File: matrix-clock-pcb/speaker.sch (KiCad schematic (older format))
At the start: 10 parts

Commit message: pcb: update pcb files
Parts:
- gave numbers to parts that had none: 10
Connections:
- net +3V3 renamed +5V
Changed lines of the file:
@@
 $EndDescr
 $Comp
-L Device:C C?
+L Device:C C14
 U 1 1 5F381B14
 P 5100 3900
-F 0 "C?" V 5050 3800 50  0000 C CNN
+F 0 "C14" V 5050 3800 50  0000 C CNN
 F 1 "1uf" V 4939 3900 50  0000 C CNN
 F 2 "Capacitor_SMD:C_0402_1005Metric" H 5138 3750 50  0001 C CNN
@@
 $EndComp
 $Comp
-L Device:R R?
+L Device:R R13
 U 1 1 5F3825B3
 P 5800 4250
-F 0 "R?" V 5700 4250 50  0000 C CNN
+F 0 "R13" V 5700 4250 50  0000 C CNN
 F 1 "20k" V 5900 4250 50  0000 C CNN
 F 2 "Resistor_SMD:R_0402_1005Metric" V 5730 4250 50  0001 C CNN
@@
 	5400 4000 5400 4250
 $Comp
-L Connector_Generic:Conn_01x02 J?
+L Connector_Generic:Conn_01x02 J5
 U 1 1 5F38725C
 P 6900 3900
-F 0 "J?" H 6980 3892 50  0000 L CNN
+F 0 "J5" H 6980 3892 50  0000 L CNN
 F 1 "Speaker" H 6980 3801 50  0000 L CNN
 F 2 "Connector_PinHeader_2.54mm:PinHeader_1x02_P2.54mm_Vertical" H 6900 3900 50  0001 C CNN
@@
 	5650 4250 5400 4250
 $Comp
-L Device:R R?
+L Device:R R12
 U 1 1 5F388BFA
 P 5250 4250
-F 0 "R?" V 5150 4250 50  0000 C CNN
+F 0 "R12" V 5150 4250 50  0000 C CNN
 F 1 "20k" V 5350 4250 50  0000 C CNN
 F 2 "Resistor_SMD:R_0402_1005Metric" V 5180 4250 50  0001 C CNN
@@
 Connection ~ 5400 4250
 $Comp
-L Device:C C?
+L Device:C C13
 U 1 1 5F389470
 P 4950 4250
-F 0 "C?" V 4900 4350 50  0000 C CNN
+F 0 "C13" V 4900 4350 50  0000 C CNN
 F 1 "0.39uf" V 4789 4250 50  0000 C CNN
 F 2 "Capacitor_SMD:C_0402_1005Metric" H 4988 4100 50  0001 C CNN
@@
 INPUT
 $Comp
-L power:GND #PWR?
+L power:GND #PWR0136
 U 1 1 5F38A0EB
 P 6100 3800
-F 0 "#PWR?" H 6100 3550 50  0001 C CNN
+F 0 "#PWR0136" H 6100 3550 50  0001 C CNN
 F 1 "GND" V 6105 3672 50  0000 R CNN
 F 2 "" H 6100 3800 50  0001 C CNN
@@
 $EndComp
 $Comp
-L power:GND #PWR?
+L power:GND #PWR0137
 U 1 1 5F38A766
 P 4950 3900
-F 0 "#PWR?" H 4950 3650 50  0001 C CNN
+F 0 "#PWR0137" H 4950 3650 50  0001 C CNN
 F 1 "GND" V 4955 3772 50  0000 R CNN
 F 2 "" H 4950 3900 50  0001 C CNN
@@
 $EndBitmap
 $Comp
-L mylib:TC8002D U?
+L mylib:TC8002D U7
 U 1 1 5F5572A6
 P 5750 3850
-F 0 "U?" H 5800 4225 50  0000 C CNN
+F 0 "U7" H 5800 4225 50  0000 C CNN
 F 1 "TC8002D" H 5800 4134 50  0000 C CNN
 F 2 "Package_SO:SOIC-8_3.9x4.9mm_P1.27mm" H 5850 3850 50  0001 C CNN
@@
 $EndComp
 $Comp
-L power:+3.3V #PWR?
-U 1 1 5F558480
-P 6100 3900
-F 0 "#PWR?" H 6100 3750 50  0001 C CNN
-F 1 "+3.3V" V 6115 4028 50  0000 L CNN
-F 2 "" H 6100 3900 50  0001 C CNN
-F 3 "" H 6100 3900 50  0001 C CNN
-	1    6100 3900
-	0    1    1    0
-$EndComp
-$Comp
-L Device:C C?
+L Device:C C11
 U 1 1 5F55C734
 P 4200 4550
-F 0 "C?" H 4250 4450 50  0000 C CNN
+F 0 "C11" H 4250 4450 50  0000 C CNN
 F 1 "0.39uf" H 4050 4650 50  0000 C CNN
 F 2 "Capacitor_SMD:C_0402_1005Metric" H 4238 4400 50  0001 C CNN
@@
 $EndComp
 $Comp
-L Device:R R?
+L Device:R R10
 U 1 1 5F55CDA5
 P 4050 4250
-F 0 "R?" V 3950 4250 50  0000 C CNN
+F 0 "R10" V 3950 4250 50  0000 C CNN
 F 1 "20k" V 4150 4250 50  0000 C CNN
 F 2 "Resistor_SMD:R_0402_1005Metric" V 3980 4250 50  0001 C CNN
@@
 $EndComp
 $Comp
-L Device:R R?
+L Device:R R11
 U 1 1 5F55D483
 P 4450 4250
-F 0 "R?" V 4350 4250 50  0000 C CNN
+F 0 "R11" V 4350 4250 50  0000 C CNN
 F 1 "20k" V 4550 4250 50  0000 C CNN
 F 2 "Resistor_SMD:R_0402_1005Metric" V 4380 4250 50  0001 C CNN
@@
 $EndComp
 $Comp
-L Device:C C?
+L Device:C C12
 U 1 1 5F55D853
 P 4600 4550
-F 0 "C?" H 4650 4450 50  0000 C CNN
+F 0 "C12" H 4650 4450 50  0000 C CNN
 F 1 "0.39uf" H 4450 4650 50  0000 C CNN
 F 2 "Capacitor_SMD:C_0402_1005Metric" H 4638 4400 50  0001 C CNN
@@
 	4600 4800 4600 4700
 $Comp
-L power:GND #PWR?
+L power:GND #PWR0139
 U 1 1 5F55FC0C
 P 4400 4800
-F 0 "#PWR?" H 4400 4550 50  0001 C CNN
+F 0 "#PWR0139" H 4400 4550 50  0001 C CNN
 F 1 "GND" V 4405 4672 50  0000 R CNN
 F 2 "" H 4400 4800 50  0001 C CNN
@@
 Wire Wire Line
 	4400 4800 4600 4800
+$Comp
+L power:+5V #PWR0138
+U 1 1 5FACCCCA
+P 6100 3900
+F 0 "#PWR0138" H 6100 3750 50  0001 C CNN
+F 1 "+5V" V 6115 4028 50  0000 L CNN
+F 2 "" H 6100 3900 50  0001 C CNN
+F 3 "" H 6100 3900 50  0001 C CNN
+	1    6100 3900
+	0    1    1    0
+$EndComp
 $EndSCHEMATC

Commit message: pcb: update pcb to v1.1
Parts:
- R12: value 20k -> 10k
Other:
- moved on the sheet: C11, C12, C13, C14, J5, R10, R11, R12, R13, U7
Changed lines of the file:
@@
 L Device:C C14
 U 1 1 5F381B14
-P 5100 3900
-F 0 "C14" V 5050 3800 50  0000 C CNN
-F 1 "1uf" V 4939 3900 50  0000 C CNN
-F 2 "Capacitor_SMD:C_0402_1005Metric" H 5138 3750 50  0001 C CNN
-F 3 "~" H 5100 3900 50  0001 C CNN
-	1    5100 3900
+P 6300 3800
+F 0 "C14" V 6250 3700 50  0000 C CNN
+F 1 "1uf" V 6139 3800 50  0000 C CNN
+F 2 "Capacitor_SMD:C_0402_1005Metric" H 6338 3650 50  0001 C CNN
+F 3 "~" H 6300 3800 50  0001 C CNN
+	1    6300 3800
 	0    1    1    0
 $EndComp
@@
 L Device:R R13
 U 1 1 5F3825B3
-P 5800 4250
-F 0 "R13" V 5700 4250 50  0000 C CNN
-F 1 "20k" V 5900 4250 50  0000 C CNN
-F 2 "Resistor_SMD:R_0402_1005Metric" V 5730 4250 50  0001 C CNN
-F 3 "~" H 5800 4250 50  0001 C CNN
-	1    5800 4250
+P 7000 4150
+F 0 "R13" V 6900 4150 50  0000 C CNN
+F 1 "20k" V 7100 4150 50  0000 C CNN
+F 2 "Resistor_SMD:R_0402_1005Metric" V 6930 4150 50  0001 C CNN
+F 3 "~" H 7000 4150 50  0001 C CNN
+	1    7000 4150
 	0    1    1    0
 $EndComp
 Wire Wire Line
-	5500 3800 5250 3800
-Wire Wire Line
-	5250 3800 5250 3900
-Wire Wire Line
-	5250 3900 5500 3900
-Connection ~ 5250 3900
-Text HLabel 4800 3700 0    50   Input ~ 0
+	6700 3700 6450 3700
+Wire Wire Line
+	6450 3700 6450 3800
+Wire Wire Line
+	6450 3800 6700 3800
+Connection ~ 6450 3800
+Text HLabel 6000 3600 0    50   Input ~ 0
 SHUTDOWN
 Wire Wire Line
-	5500 4000 5400 4000
-Wire Wire Line
-	5400 4000 5400 4250
+	6700 3900 6600 3900
+Wire Wire Line
+	6600 3900 6600 4150
 $Comp
 L Connector_Generic:Conn_01x02 J5
 U 1 1 5F38725C
-P 6900 3900
-F 0 "J5" H 6980 3892 50  0000 L CNN
-F 1 "Speaker" H 6980 3801 50  0000 L CNN
-F 2 "Connector_PinHeader_2.54mm:PinHeader_1x02_P2.54mm_Vertical" H 6900 3900 50  0001 C CNN
-F 3 "~" H 6900 3900 50  0001 C CNN
-	1    6900 3900
+P 8100 3800
+F 0 "J5" H 8180 3792 50  0000 L CNN
+F 1 "Speaker" H 8180 3701 50  0000 L CNN
+F 2 "Connector_PinHeader_2.54mm:PinHeader_1x02_P2.54mm_Vertical" H 8100 3800 50  0001 C CNN
+F 3 "~" H 8100 3800 50  0001 C CNN
+	1    8100 3800
 	1    0    0    -1
 $EndComp
 Wire Wire Line
-	6700 4000 6250 4000
-Wire Wire Line
-	6100 3700 6600 3700
-Wire Wire Line
-	6600 3700 6600 3900
-Wire Wire Line
-	6600 3900 6700 3900
-Wire Wire Line
-	5950 4250 6250 4250
-Wire Wire Line
-	6250 4250 6250 4000
-Connection ~ 6250 4000
-Wire Wire Line
-	6250 4000 6100 4000
-Wire Wire Line
-	5650 4250 5400 4250
+	7900 3900 7450 3900
+Wire Wire Line
+	7300 3600 7800 3600
+Wire Wire Line
+	7800 3600 7800 3800
+Wire Wire Line
+	7800 3800 7900 3800
+Wire Wire Line
+	7150 4150 7450 4150
+Wire Wire Line
+	7450 4150 7450 3900
+Connection ~ 7450 3900
+Wire Wire Line
+	7450 3900 7300 3900
+Wire Wire Line
+	6850 4150 6600 4150
 $Comp
 L Device:R R12
 U 1 1 5F388BFA
-P 5250 4250
-F 0 "R12" V 5150 4250 50  0000 C CNN
-F 1 "20k" V 5350 4250 50  0000 C CNN
-F 2 "Resistor_SMD:R_0402_1005Metric" V 5180 4250 50  0001 C CNN
-F 3 "~" H 5250 4250 50  0001 C CNN
-	1    5250 4250
+P 6450 4150
+F 0 "R12" V 6350 4150 50  0000 C CNN
+F 1 "10k" V 6550 4150 50  0000 C CNN
+F 2 "Resistor_SMD:R_0402_1005Metric" V 6380 4150 50  0001 C CNN
+F 3 "~" H 6450 4150 50  0001 C CNN
+	1    6450 4150
 	0    1    1    0
 $EndComp
-Connection ~ 5400 4250
+Connection ~ 6600 4150
 $Comp
 L Device:C C13
 U 1 1 5F389470
-P 4950 4250
-F 0 "C13" V 4900 4350 50  0000 C CNN
-F 1 "0.39uf" V 4789 4250 50  0000 C CNN
-F 2 "Capacitor_SMD:C_0402_1005Metric" H 4988 4100 50  0001 C CNN
-F 3 "~" H 4950 4250 50  0001 C CNN
-	1    4950 4250
+P 6150 4150
+F 0 "C13" V 6100 4250 50  0000 C CNN
+F 1 "0.39uf" V 5989 4150 50  0000 C CNN
+F 2 "Capacitor_SMD:C_0402_1005Metric" H 6188 4000 50  0001 C CNN
+F 3 "~" H 6150 4150 50  0001 C CNN
+	1    6150 4150
 	0    1    1    0
 $EndComp
-Text HLabel 3900 4250 0    50   Input ~ 0
+Text HLabel 5100 4150 0    50   Input ~ 0
 INPUT
 $Comp
 L power:GND #PWR0136
 U 1 1 5F38A0EB
-P 6100 3800
-F 0 "#PWR0136" H 6100 3550 50  0001 C CNN
-F 1 "GND" V 6105 3672 50  0000 R CNN
-F 2 "" H 6100 3800 50  0001 C CNN
-F 3 "" H 6100 3800 50  0001 C CNN
-	1    6100 3800
+P 7300 3700
+F 0 "#PWR0136" H 7300 3450 50  0001 C CNN
+F 1 "GND" V 7305 3572 50  0000 R CNN
+F 2 "" H 7300 3700 50  0001 C CNN
+F 3 "" H 7300 3700 50  0001 C CNN
+	1    7300 3700
 	0    -1   -1   0
 $EndComp
@@
 L power:GND #PWR0137
 U 1 1 5F38A766
-P 4950 3900
-F 0 "#PWR0137" H 4950 3650 50  0001 C CNN
-F 1 "GND" V 4955 3772 50  0000 R CNN
-F 2 "" H 4950 3900 50  0001 C CNN
-F 3 "" H 4950 3900 50  0001 C CNN
-	1    4950 3900
+P 6150 3800
+F 0 "#PWR0137" H 6150 3550 50  0001 C CNN
+F 1 "GND" V 6155 3672 50  0000 R CNN
+F 2 "" H 6150 3800 50  0001 C CNN
+F 3 "" H 6150 3800 50  0001 C CNN
+	1    6150 3800
 	0    1    1    0
 $EndComp
 Wire Wire Line
-	4800 3700 5500 3700
+	6000 3600 6700 3600
 $Bitmap
-Pos 1900 4000
+Pos 3100 3900
 Scale 1.500000
 Data
@@
 L mylib:TC8002D U7
 U 1 1 5F5572A6
-P 5750 3850
-F 0 "U7" H 5800 4225 50  0000 C CNN
-F 1 "TC8002D" H 5800 4134 50  0000 C CNN
-F 2 "Package_SO:SOIC-8_3.9x4.9mm_P1.27mm" H 5850 3850 50  0001 C CNN
-F 3 "" H 5750 3850 50  0001 C CNN
-	1    5750 3850
+P 6950 3750
+F 0 "U7" H 7000 4125 50  0000 C CNN
+F 1 "TC8002D" H 7000 4034 50  0000 C CNN
+F 2 "Package_SO:SOIC-8_3.9x4.9mm_P1.27mm" H 7050 3750 50  0001 C CNN
+F 3 "" H 6950 3750 50  0001 C CNN
+	1    6950 3750
 	1    0    0    -1
 $EndComp
@@
 L Device:C C11
 U 1 1 5F55C734
-P 4200 4550
-F 0 "C11" H 4250 4450 50  0000 C CNN
-F 1 "0.39uf" H 4050 4650 50  0000 C CNN
-F 2 "Capacitor_SMD:C_0402_1005Metric" H 4238 4400 50  0001 C CNN
-F 3 "~" H 4200 4550 50  0001 C CNN
-	1    4200 4550
+P 5400 4450
+F 0 "C11" H 5450 4350 50  0000 C CNN
+F 1 "0.39uf" H 5250 4550 50  0000 C CNN
+F 2 "Capacitor_SMD:C_0402_1005Metric" H 5438 4300 50  0001 C CNN
+F 3 "~" H 5400 4450 50  0001 C CNN
+	1    5400 4450
 	-1   0    0    1
 $EndComp
@@
 L Device:R R10
 U 1 1 5F55CDA5
-P 4050 4250
-F 0 "R10" V 3950 4250 50  0000 C CNN
-F 1 "20k" V 4150 4250 50  0000 C CNN
-F 2 "Resistor_SMD:R_0402_1005Metric" V 3980 4250 50  0001 C CNN
-F 3 "~" H 4050 4250 50  0001 C CNN
-	1    4050 4250
-	0    1    1    0
-$EndComp
-$Comp
-L Device:R R11
-U 1 1 5F55D483
-P 4450 4250
-F 0 "R11" V 4350 4250 50  0000 C CNN
-F 1 "20k" V 4550 4250 50  0000 C CNN
-F 2 "Resistor_SMD:R_0402_1005Metric" V 4380 4250 50  0001 C CNN
-F 3 "~" H 4450 4250 50  0001 C CNN
-	1    4450 4250
+P 5250 4150
+F 0 "R10" V 5150 4150 50  0000 C CNN
+F 1 "20k" V 5350 4150 50  0000 C CNN
+F 2 "Resistor_SMD:R_0402_1005Metric" V 5180 4150 50  0001 C CNN
+F 3 "~" H 5250 4150 50  0001 C CNN
+	1    5250 4150
 	0    1    1    0
 $EndComp
@@
 L Device:C C12
 U 1 1 5F55D853
-P 4600 4550
-F 0 "C12" H 4650 4450 50  0000 C CNN
-F 1 "0.39uf" H 4450 4650 50  0000 C CNN
-F 2 "Capacitor_SMD:C_0402_1005Metric" H 4638 4400 50  0001 C CNN
-F 3 "~" H 4600 4550 50  0001 C CNN
-	1    4600 4550
+P 5800 4450
+F 0 "C12" H 5850 4350 50  0000 C CNN
+F 1 "0.39uf" H 5650 4550 50  0000 C CNN
+F 2 "Capacitor_SMD:C_0402_1005Metric" H 5838 4300 50  0001 C CNN
+F 3 "~" H 5800 4450 50  0001 C CNN
+	1    5800 4450
 	-1   0    0    1
 $EndComp
 Wire Wire Line
-	4200 4250 4300 4250
-Wire Wire Line
-	4600 4250 4800 4250
-Wire Wire Line
-	4600 4400 4600 4250
-Connection ~ 4600 4250
-Wire Wire Line
-	4200 4400 4200 4250
-Connection ~ 4200 4250
-Wire Wire Line
-	4200 4700 4200 4800
-Wire Wire Line
-	4200 4800 4400 4800
-Wire Wire Line
-	4600 4800 4600 4700
+	5400 4150 5500 4150
+Wire Wire Line
+	5800 4150 6000 4150
+Wire Wire Line
+	5800 4300 5800 4150
+Wire Wire Line
+	5400 4300 5400 4150
+Connection ~ 5400 4150
+Wire Wire Line
+	5400 4600 5400 4700
+Wire Wire Line
+	5400 4700 5600 4700
+Wire Wire Line
+	5800 4700 5800 4600
 $Comp
 L power:GND #PWR0139
 U 1 1 5F55FC0C
-P 4400 4800
-F 0 "#PWR0139" H 4400 4550 50  0001 C CNN
-F 1 "GND" V 4405 4672 50  0000 R CNN
-F 2 "" H 4400 4800 50  0001 C CNN
-F 3 "" H 4400 4800 50  0001 C CNN
-	1    4400 4800
+P 5600 4700
+F 0 "#PWR0139" H 5600 4450 50  0001 C CNN
+F 1 "GND" V 5605 4572 50  0000 R CNN
+F 2 "" H 5600 4700 50  0001 C CNN
+F 3 "" H 5600 4700 50  0001 C CNN
+	1    5600 4700
 	1    0    0    -1
 $EndComp
-Connection ~ 4400 4800
-Wire Wire Line
-	4400 4800 4600 4800
+Connection ~ 5600 4700
+Wire Wire Line
+	5600 4700 5800 4700
 $Comp
 L power:+5V #PWR0138
 U 1 1 5FACCCCA
-P 6100 3900
-F 0 "#PWR0138" H 6100 3750 50  0001 C CNN
-F 1 "+5V" V 6115 4028 50  0000 L CNN
-F 2 "" H 6100 3900 50  0001 C CNN
-F 3 "" H 6100 3900 50  0001 C CNN
-	1    6100 3900
+P 7300 3800
+F 0 "#PWR0138" H 7300 3650 50  0001 C CNN
+F 1 "+5V" V 7315 3928 50  0000 L CNN
+F 2 "" H 7300 3800 50  0001 C CNN
+F 3 "" H 7300 3800 50  0001 C CNN
+	1    7300 3800
 	0    1    1    0
 $EndComp
+Connection ~ 5800 4150
+$Comp
+L Device:R R11
+U 1 1 5F55D483
+P 5650 4150
+F 0 "R11" V 5550 4150 50  0000 C CNN
+F 1 "20k" V 5750 4150 50  0000 C CNN
+F 2 "Resistor_SMD:R_0402_1005Metric" V 5580 4150 50  0001 C CNN
+F 3 "~" H 5650 4150 50  0001 C CNN
+	1    5650 4150
+	0    1    1    0
+$EndComp

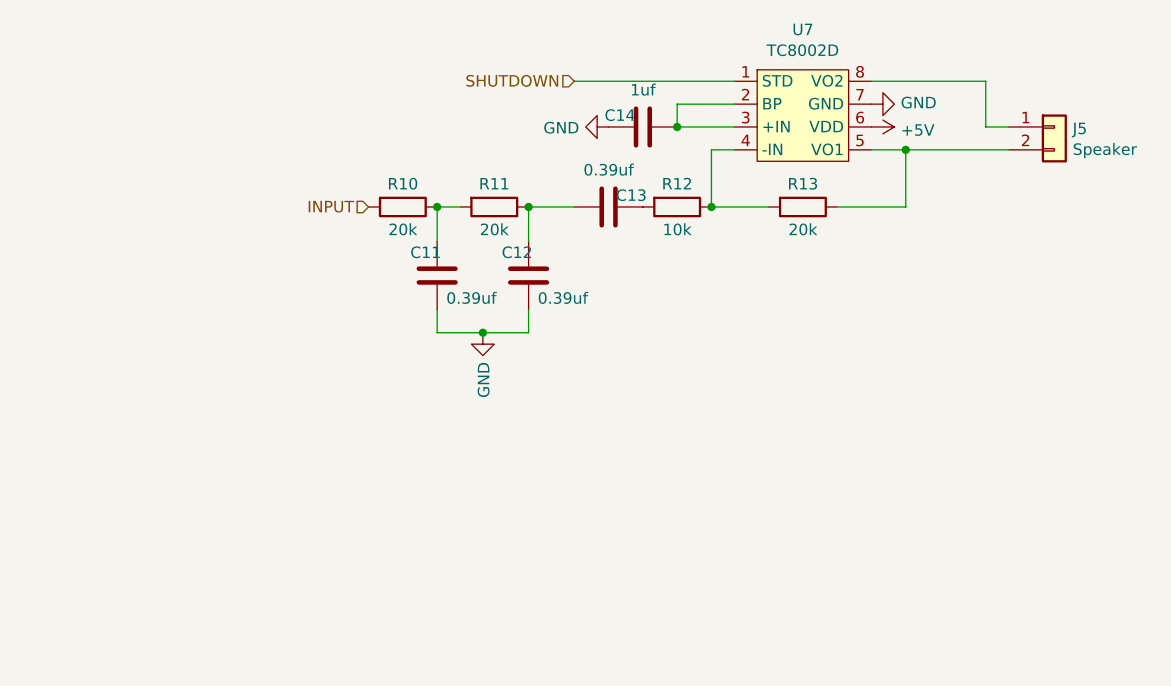
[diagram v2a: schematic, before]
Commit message: fix(pcb): update pcb layout
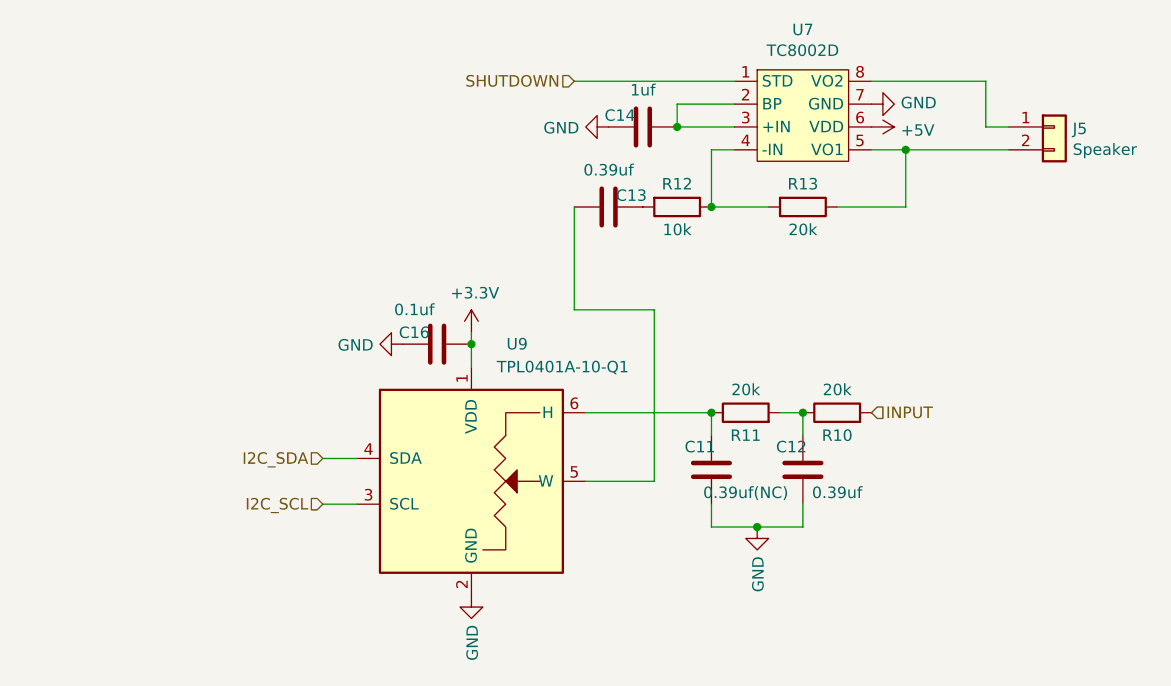
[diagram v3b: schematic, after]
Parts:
- added C16: 0.1uf, Capacitor_SMD:C_0402_1005Metric, symbol Device:C
- added U9: TPL0401A-10-Q1, Package_TO_SOT_SMD:Texas_R-PDSO-G6, symbol Potentiometer_Digital:TPL0401A-10-Q1
- C11: value 0.39uf -> 0.39uf(NC)
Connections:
- net GND: now also C16.2, U9.2 (GND)
- net at R10.1, R11.2: now also C12.2; no longer C11.2
- new net: C13.2, U9.5 (W)
- new net: C11.2, R11.1, U9.6 (H)
- new net +3V3: C16.1, U9.1 (VDD)
- new net I2C_SCL: U9.3 (SCL)
- new net I2C_SDA: U9.4 (SDA)
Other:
- moved on the sheet: C11, C12, R10, R11
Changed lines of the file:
@@
 $Descr A4 11693 8268
 encoding utf-8
-Sheet 3 3
+Sheet 2 3
 Title "speaker"
 Date "2020-11-02"
@@
 	0    1    1    0
 $EndComp
-Text HLabel 5100 4150 0    50   Input ~ 0
+Text HLabel 7300 5050 2    50   Input ~ 0
 INPUT
 $Comp
@@
 $EndComp
 $Comp
-L Device:C C11
-U 1 1 5F55C734
-P 5400 4450
-F 0 "C11" H 5450 4350 50  0000 C CNN
-F 1 "0.39uf" H 5250 4550 50  0000 C CNN
-F 2 "Capacitor_SMD:C_0402_1005Metric" H 5438 4300 50  0001 C CNN
-F 3 "~" H 5400 4450 50  0001 C CNN
-	1    5400 4450
-	-1   0    0    1
-$EndComp
-$Comp
 L Device:R R10
 U 1 1 5F55CDA5
-P 5250 4150
-F 0 "R10" V 5150 4150 50  0000 C CNN
-F 1 "20k" V 5350 4150 50  0000 C CNN
-F 2 "Resistor_SMD:R_0402_1005Metric" V 5180 4150 50  0001 C CNN
-F 3 "~" H 5250 4150 50  0001 C CNN
-	1    5250 4150
-	0    1    1    0
+P 7150 5050
+F 0 "R10" V 7050 5050 50  0000 C CNN
+F 1 "20k" V 7250 5050 50  0000 C CNN
+F 2 "Resistor_SMD:R_0402_1005Metric" V 7080 5050 50  0001 C CNN
+F 3 "~" H 7150 5050 50  0001 C CNN
+	1    7150 5050
+	0    -1   -1   0
 $EndComp
 $Comp
 L Device:C C12
 U 1 1 5F55D853
-P 5800 4450
-F 0 "C12" H 5850 4350 50  0000 C CNN
-F 1 "0.39uf" H 5650 4550 50  0000 C CNN
-F 2 "Capacitor_SMD:C_0402_1005Metric" H 5838 4300 50  0001 C CNN
-F 3 "~" H 5800 4450 50  0001 C CNN
-	1    5800 4450
+P 7000 5300
+F 0 "C12" H 7050 5200 50  0000 C CNN
+F 1 "0.39uf" H 6850 5400 50  0000 C CNN
+F 2 "Capacitor_SMD:C_0402_1005Metric" H 7038 5150 50  0001 C CNN
+F 3 "~" H 7000 5300 50  0001 C CNN
+	1    7000 5300
 	-1   0    0    1
 $EndComp
 Wire Wire Line
-	5400 4150 5500 4150
-Wire Wire Line
-	5800 4150 6000 4150
-Wire Wire Line
-	5800 4300 5800 4150
-Wire Wire Line
-	5400 4300 5400 4150
-Connection ~ 5400 4150
-Wire Wire Line
-	5400 4600 5400 4700
-Wire Wire Line
-	5400 4700 5600 4700
-Wire Wire Line
-	5800 4700 5800 4600
+	7000 5050 6900 5050
+Wire Wire Line
+	6600 5450 6600 5550
+Wire Wire Line
+	6600 5550 6800 5550
+Wire Wire Line
+	7000 5550 7000 5450
 $Comp
 L power:GND #PWR0139
 U 1 1 5F55FC0C
-P 5600 4700
-F 0 "#PWR0139" H 5600 4450 50  0001 C CNN
-F 1 "GND" V 5605 4572 50  0000 R CNN
-F 2 "" H 5600 4700 50  0001 C CNN
-F 3 "" H 5600 4700 50  0001 C CNN
-	1    5600 4700
+P 6800 5550
+F 0 "#PWR0139" H 6800 5300 50  0001 C CNN
+F 1 "GND" V 6805 5422 50  0000 R CNN
+F 2 "" H 6800 5550 50  0001 C CNN
+F 3 "" H 6800 5550 50  0001 C CNN
+	1    6800 5550
 	1    0    0    -1
 $EndComp
-Connection ~ 5600 4700
-Wire Wire Line
-	5600 4700 5800 4700
+Connection ~ 6800 5550
+Wire Wire Line
+	6800 5550 7000 5550
 $Comp
 L power:+5V #PWR0138
@@
 	0    1    1    0
 $EndComp
-Connection ~ 5800 4150
 $Comp
 L Device:R R11
 U 1 1 5F55D483
-P 5650 4150
-F 0 "R11" V 5550 4150 50  0000 C CNN
-F 1 "20k" V 5750 4150 50  0000 C CNN
-F 2 "Resistor_SMD:R_0402_1005Metric" V 5580 4150 50  0001 C CNN
-F 3 "~" H 5650 4150 50  0001 C CNN
-	1    5650 4150
+P 6750 5050
+F 0 "R11" V 6650 5050 50  0000 C CNN
+F 1 "20k" V 6850 5050 50  0000 C CNN
+F 2 "Resistor_SMD:R_0402_1005Metric" V 6680 5050 50  0001 C CNN
+F 3 "~" H 6750 5050 50  0001 C CNN
+	1    6750 5050
+	0    -1   -1   0
+$EndComp
+$Comp
+L Potentiometer_Digital:TPL0401A-10-Q1 U9
+U 1 1 60481B78
+P 5550 5350
+F 0 "U9" H 5750 5950 50  0000 C CNN
+F 1 "TPL0401A-10-Q1" H 5950 5850 50  0000 C CNN
+F 2 "Package_TO_SOT_SMD:Texas_R-PDSO-G6" H 5600 4900 50  0001 L CNN
+F 3 "http://www.ti.com/lit/ds/symlink/tpl0401a-10-q1.pdf" H 5600 4800 50  0001 L CNN
+	1    5550 5350
+	1    0    0    -1
+$EndComp
+Text HLabel 4900 5250 0    50   Input ~ 0
+I2C_SDA
+Text HLabel 4900 5450 0    50   Input ~ 0
+I2C_SCL
+Wire Wire Line
+	4900 5450 5050 5450
+Wire Wire Line
+	4900 5250 5050 5250
+$Comp
+L power:GND #PWR08
+U 1 1 6048B3E5
+P 5550 5850
+F 0 "#PWR08" H 5550 5600 50  0001 C CNN
+F 1 "GND" V 5555 5722 50  0000 R CNN
+F 2 "" H 5550 5850 50  0001 C CNN
+F 3 "" H 5550 5850 50  0001 C CNN
+	1    5550 5850
+	1    0    0    -1
+$EndComp
+Wire Wire Line
+	6600 5150 6600 5050
+Wire Wire Line
+	7000 5150 7000 5050
+Connection ~ 7000 5050
+Wire Wire Line
+	6050 5050 6600 5050
+Connection ~ 6600 5050
+Wire Wire Line
+	6000 4150 6000 4600
+Wire Wire Line
+	6000 4600 6350 4600
+Wire Wire Line
+	6350 4600 6350 5350
+Wire Wire Line
+	6350 5350 6050 5350
+$Comp
+L Device:C C11
+U 1 1 5F55C734
+P 6600 5300
+F 0 "C11" H 6650 5200 50  0000 C CNN
+F 1 "0.39uf(NC)" H 6450 5400 50  0000 C CNN
+F 2 "Capacitor_SMD:C_0402_1005Metric" H 6638 5150 50  0001 C CNN
+F 3 "~" H 6600 5300 50  0001 C CNN
+	1    6600 5300
+	-1   0    0    1
+$EndComp
+$Comp
+L Device:C C16
+U 1 1 604C6D8F
+P 5400 4750
+F 0 "C16" V 5350 4650 50  0000 C CNN
+F 1 "0.1uf" V 5250 4650 50  0000 C CNN
+F 2 "Capacitor_SMD:C_0402_1005Metric" H 5438 4600 50  0001 C CNN
+F 3 "~" H 5400 4750 50  0001 C CNN
+	1    5400 4750
 	0    1    1    0
 $EndComp
+$Comp
+L power:GND #PWR09
+U 1 1 604C82D6
+P 5250 4750
+F 0 "#PWR09" H 5250 4500 50  0001 C CNN
+F 1 "GND" V 5255 4622 50  0000 R CNN
+F 2 "" H 5250 4750 50  0001 C CNN
+F 3 "" H 5250 4750 50  0001 C CNN
+	1    5250 4750
+	0    1    1    0
+$EndComp
+Wire Wire Line
+	5550 4700 5550 4750
+Connection ~ 5550 4750
+Wire Wire Line
+	5550 4750 5550 4850
+$Comp
+L power:+3.3V #PWR07
+U 1 1 6048AACC
+P 5550 4700
+F 0 "#PWR07" H 5550 4550 50  0001 C CNN
+F 1 "+3.3V" H 5565 4873 50  0000 C CNN
+F 2 "" H 5550 4700 50  0001 C CNN
+F 3 "" H 5550 4700 50  0001 C CNN
+	1    5550 4700
+	1    0    0    -1
+$EndComp
 $EndSCHEMATC
